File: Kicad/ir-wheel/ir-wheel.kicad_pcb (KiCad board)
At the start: 2 copper layers, 58 x 25 mm, 10 parts, among them IC1 TTE-OPB606, IC2 TTE-OPB606, K1 MOLEX-MICRO-LATCH-03-RIGHT-AN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, K2 MOLEX-MICRO-LATCH-03-RIGHT-AN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

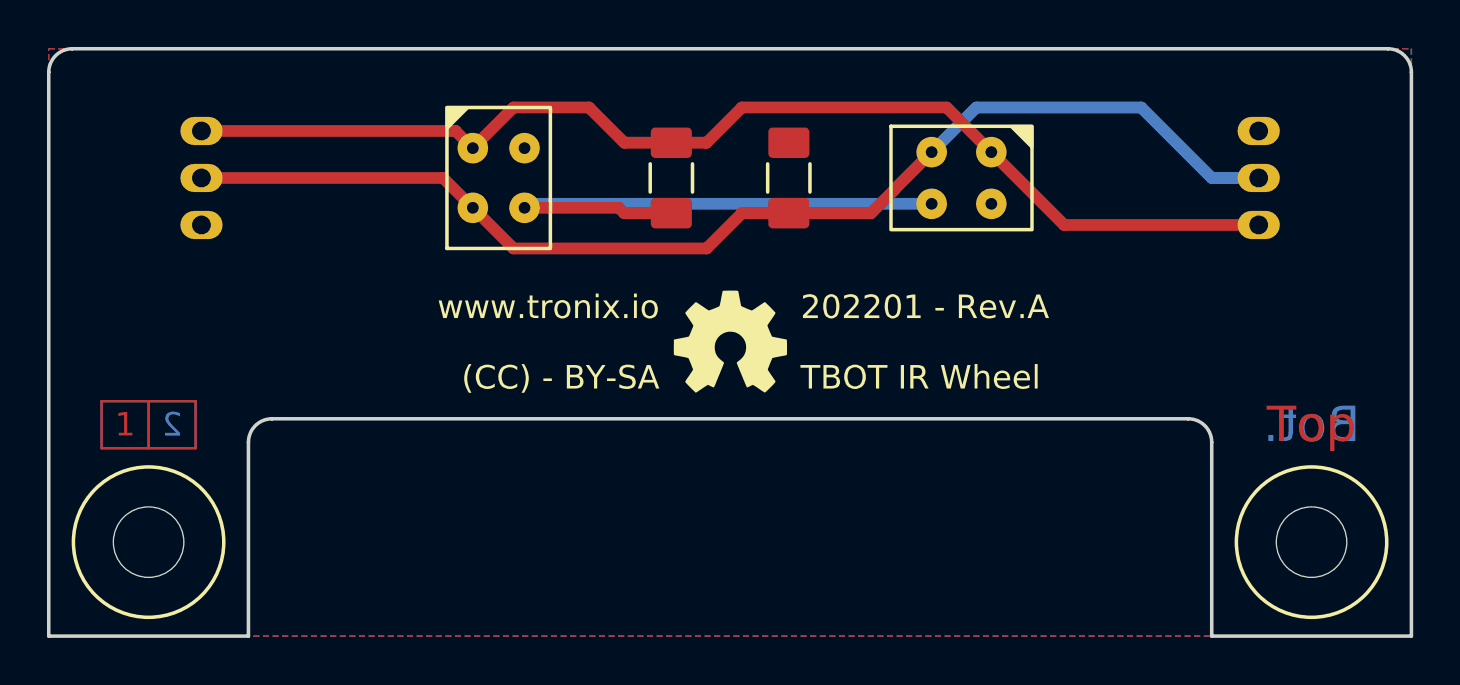
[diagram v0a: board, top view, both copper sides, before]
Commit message: Add IR Wheel
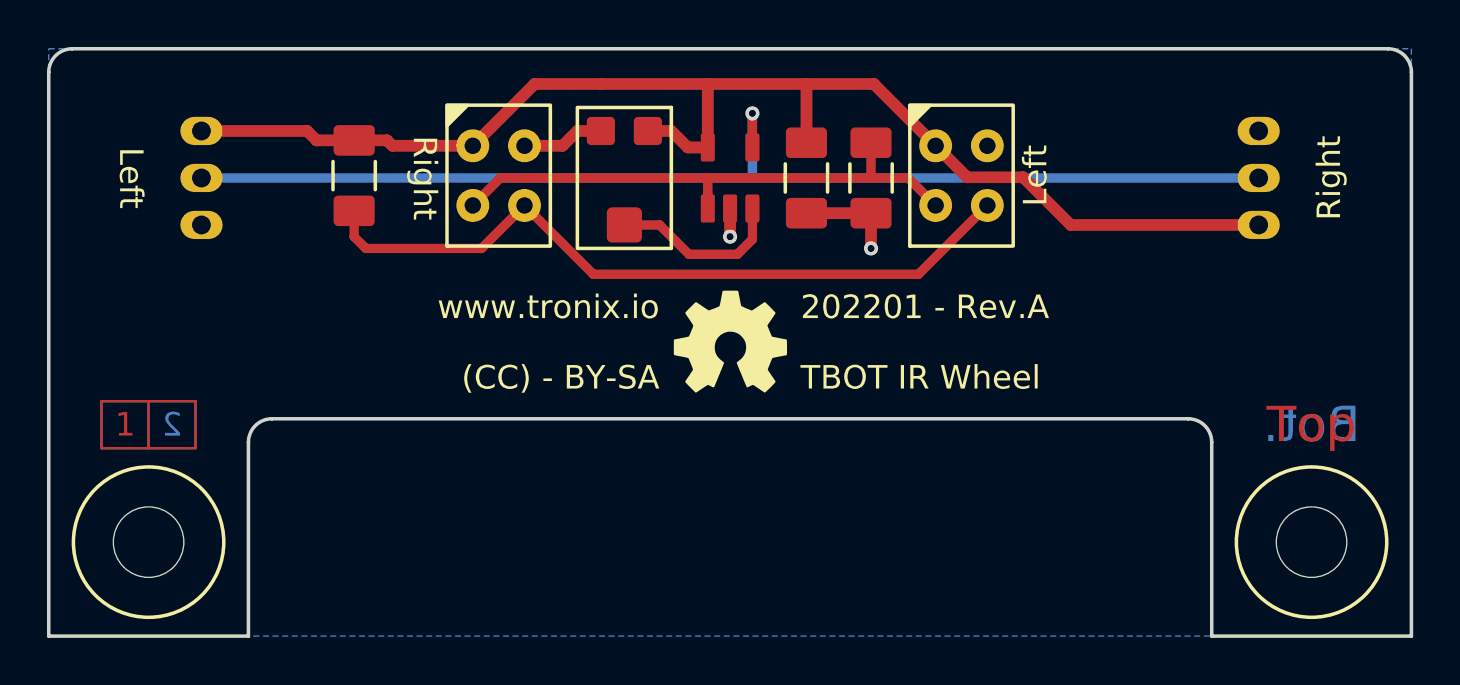
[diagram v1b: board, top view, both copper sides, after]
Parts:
- added C1: 100n, tronixio:CAPACITOR-1206, F.Cu at (132.2, 80.5)
- added P1: BOURNS-TC33X-1K, tronixio:zzzTC33X, F.Cu at (124.5, 80.5)
- added U1: MICROCHIP-MCP6541-SOT-23, tronixio:SOT-23-5, F.Cu at (129.0, 80.5)
- IC1, IC2: footprint tronixio:zzzOPB-606 -> tronixio:zzOPB-606
- moved K1 45.2 mm to (106.5, 78.5), turned to -90 degrees
- moved K2 45.2 mm to (151.5, 82.5), turned to 90 degrees
- moved R1 13.5 mm to (113.0, 80.4)
- moved R2 3.50 mm to (135.0, 80.5), turned to 90 degrees
- moved IC1 0.10 mm to (119.2, 80.4)
- moved IC2 0.10 mm to (138.8, 80.4), turned to 0 degrees
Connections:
- K1 pad 2: Net-(IC1-Pad4) -> Net-(K1-Pad2)
- K2 pad 2: Net-(IC1-Pad4) -> Net-(K1-Pad2)
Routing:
- net Net-(K1-Pad2): track 0.00 -> 49.2 mm, vias 0 -> 1
- net Net-(IC1-Pad4): track 50.0 -> 23.5 mm
- net GND: track 0.00 -> 8.96 mm, vias 0 -> 2
- net Net-(IC1-Pad1): track 23.5 -> 31.4 mm
- net +5V: track 49.3 -> 56.9 mm
- net Net-(U1-Pad3): track 0.00 -> 7.54 mm
- removed copper zone on F.Cu, net GND
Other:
- board text added: "IC2: update y+1 19.5 -> 19.6"
- board text added: "Left"
- board text added: "OPB606: update dirll 0,5 -> .7"
- board text added: "Right"

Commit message: Update IR WHEEL
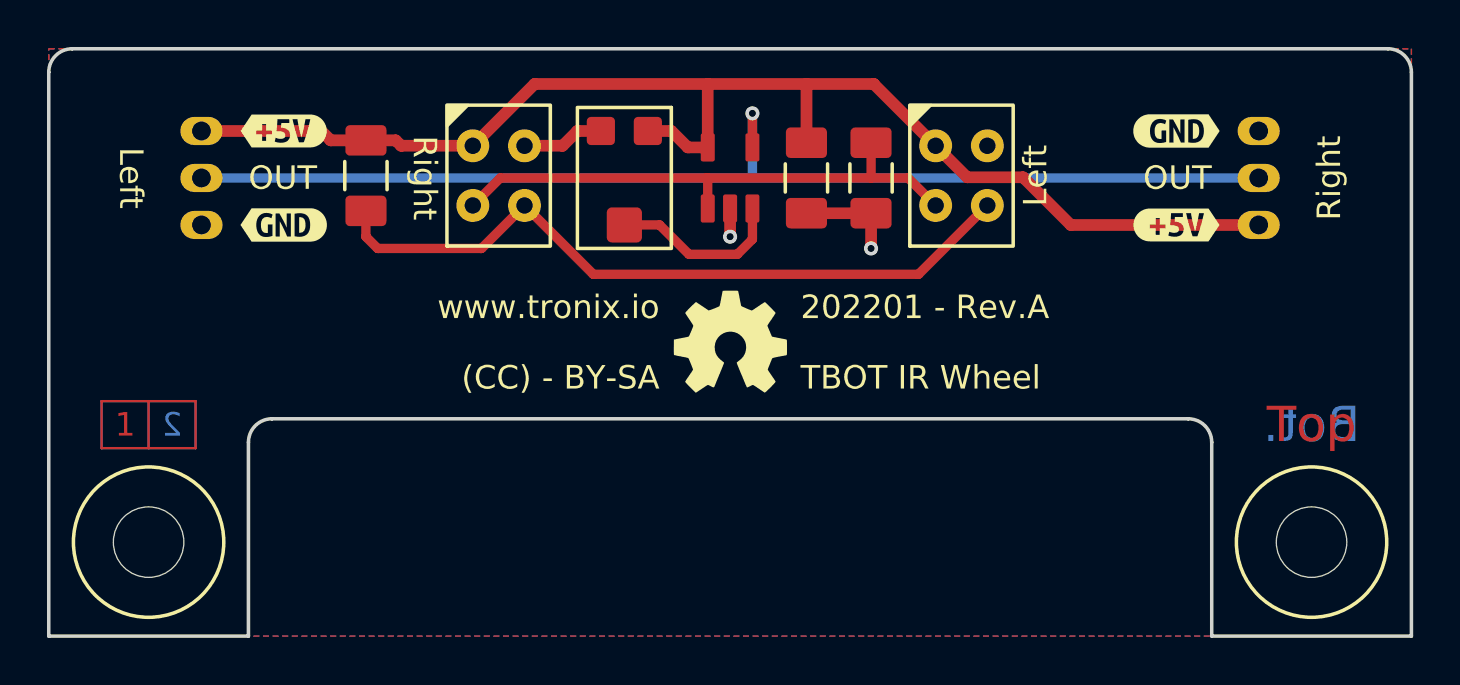
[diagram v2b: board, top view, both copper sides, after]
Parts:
- added kibuzzard-627E9F99: G***, kibuzzard-627E9F99, F.Cu at (110.0, 82.5)
- added kibuzzard-627EA1B6: G***, kibuzzard-627EA1B6, F.Cu at (110.0, 78.5)
- added kibuzzard-627EA1D4: G***, kibuzzard-627EA1D4, F.Cu at (148.0, 78.5)
- added kibuzzard-627EA1EB: G***, kibuzzard-627EA1EB, F.Cu at (148.0, 82.5)
- K1: value MOLEX-MICRO-LATCH-03-RIGHT-ANGLE -> RIGHT
- K2: value MOLEX-MICRO-LATCH-03-RIGHT-ANGLE -> LEFT
- moved R1 0.50 mm to (113.5, 80.4)
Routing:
- added copper zone on F.Cu, net GND
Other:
- board text added: "OUT"

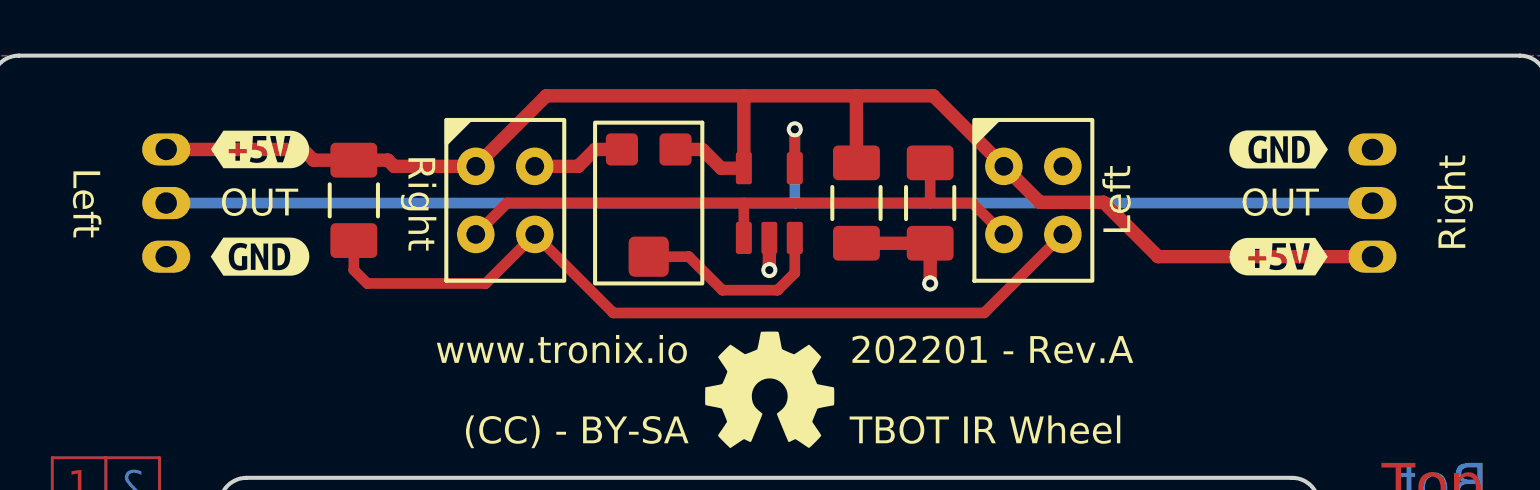
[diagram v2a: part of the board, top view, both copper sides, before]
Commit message: Update IR WHEEL
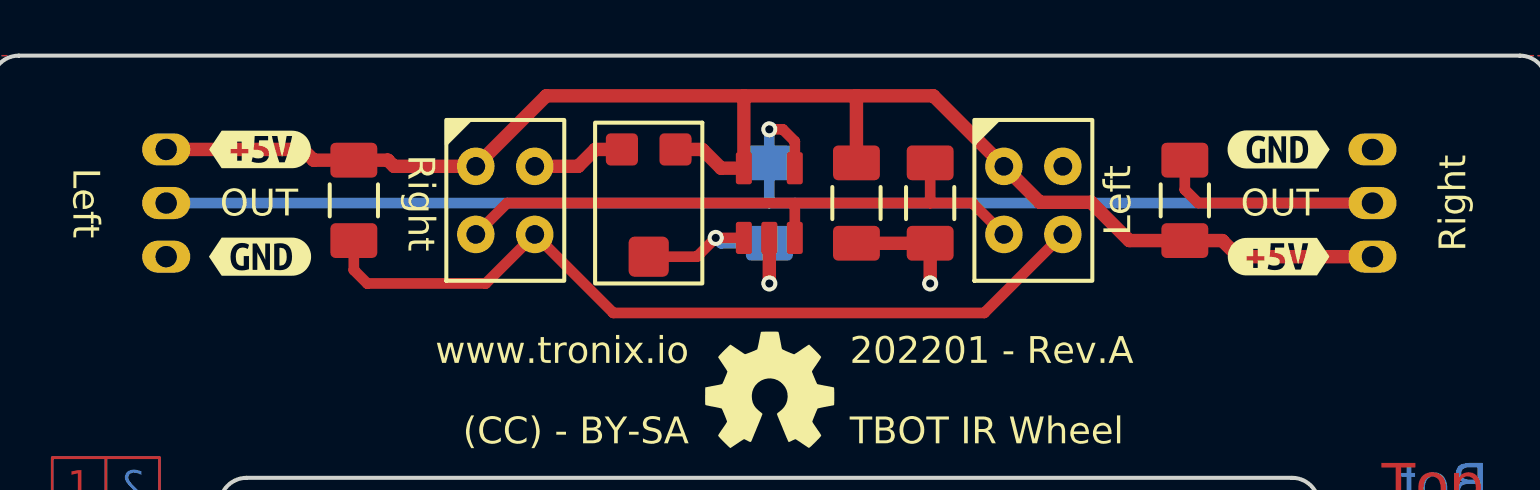
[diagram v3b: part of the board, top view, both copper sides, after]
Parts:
- removed kibuzzard-627E9F99: G***, kibuzzard-627E9F99
- removed kibuzzard-627EA1B6: G***, kibuzzard-627EA1B6
- removed kibuzzard-627EA1D4: G***, kibuzzard-627EA1D4
- removed kibuzzard-627EA1EB: G***, kibuzzard-627EA1EB
- added R3: 10K, tronixio:RESISTOR-1206, F.Cu at (144.5, 80.4)
- added R4: 10K, tronixio:RESISTOR-1206, B.Cu at (129.0, 80.5)
- added kibuzzard-62813E44: G***, kibuzzard-62813E44, F.Cu at (110.0, 82.5)
- added kibuzzard-62813E52: G***, kibuzzard-62813E52, F.Cu at (110.0, 78.5)
- added kibuzzard-62813E5A: G***, kibuzzard-62813E5A, F.Cu at (148.0, 78.5)
- added kibuzzard-62813E63: G***, kibuzzard-62813E63, F.Cu at (148.0, 82.5)
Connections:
- U1 pad 1: Net-(IC1-Pad4) -> Net-(P1-Pad2)
- U1 pad 3: Net-(P1-Pad2) -> Net-(IC1-Pad4)
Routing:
- net Net-(K1-Pad2): track 49.2 -> 58.2 mm
- net Net-(P1-Pad2): track 7.54 -> 5.92 mm, vias 0 -> 1
- net GND: track 8.96 -> 9.46 mm

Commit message: Update
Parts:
- added C2: 1µ, tronixio:CAPACITOR-1206, B.Cu at (132.2, 80.5)
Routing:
- net +5V: track 56.9 -> 58.4 mm, vias 0 -> 1
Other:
- board text removed: "OPB606: update dirll 0,5 -> .7"
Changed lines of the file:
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@@
     (attr board_only exclude_from_pos_files exclude_from_bom)
     (fp_text reference "kibuzzard-62813E52" (at 0 -3.748088) (layer "F.SilkS") hide
-      (effects (font (size 0 0)))
+      (effects (font (size 0 0) (thickness 0.15)))
     )
     (fp_text value "G***" (at 0 3.748088) (layer "F.SilkS") hide
-      (effects (font (size 0 0)))
+      (effects (font (size 0 0) (thickness 0.15)))
     )
     (fp_poly (pts
@@
     (attr board_only exclude_from_pos_files exclude_from_bom)
     (fp_text reference "kibuzzard-62813E5A" (at 0 -3.7592) (layer "F.SilkS") hide
-      (effects (font (size 0 0)))
+      (effects (font (size 0 0) (thickness 0.15)))
     )
     (fp_text value "G***" (at 0 3.7592) (layer "F.SilkS") hide
-      (effects (font (size 0 0)))
+      (effects (font (size 0 0) (thickness 0.15)))
     )
     (fp_poly (pts
@@
     (attr board_only exclude_from_pos_files exclude_from_bom)
     (fp_text reference "kibuzzard-62813E44" (at 0 -3.7592) (layer "F.SilkS") hide
-      (effects (font (size 0 0)))
+      (effects (font (size 0 0) (thickness 0.15)))
     )
     (fp_text value "G***" (at 0 3.7592) (layer "F.SilkS") hide
-      (effects (font (size 0 0)))
+      (effects (font (size 0 0) (thickness 0.15)))
     )
     (fp_poly (pts
@@
     (attr board_only exclude_from_pos_files exclude_from_bom)
     (fp_text reference "kibuzzard-62813E63" (at 0 -3.748088) (layer "F.SilkS") hide
-      (effects (font (size 0 0)))
+      (effects (font (size 0 0) (thickness 0.15)))
     )
     (fp_text value "G***" (at 0 3.748088) (layer "F.SilkS") hide
-      (effects (font (size 0 0)))
+      (effects (font (size 0 0) (thickness 0.15)))
     )
     (fp_poly (pts
@@
     )
   )
+  (footprint "tronixio:CAPACITOR-1206" (layer "B.Cu")
+    (at 132.25 80.5 -90)
+    (property "Sheetfile" "ir-wheel.kicad_sch")
+    (property "Sheetname" "")
+    (zone_connect 2)
+    (attr smd)
+    (fp_text reference "C2" (at 0 2 90) (layer "B.Fab")
+      (effects (font (size 1 1) (thickness 0.15)) (justify mirror))
+    )
+    (fp_text value "1µ" (at 0 -2 90) (layer "B.Fab")
+      (effects (font (size 1 1) (thickness 0.15)) (justify mirror))
+    )
+    (fp_line (start -0.6 0.9) (end 0.6 0.9) (layer "B.SilkS") (width 0.15))
+    (fp_line (start -0.6 -0.9) (end 0.6 -0.9) (layer "B.SilkS") (width 0.15))
+    (fp_rect (start -2.3 -1) (end 2.3 1) (layer "B.CrtYd") (width 0.05) (fill none))
+    (fp_rect (start 1.2 -0.8) (end 1.5 0.8) (layer "B.Fab") (width 0.1) (fill solid))
+    (fp_rect (start -1.2 -0.8) (end 1.2 0.8) (layer "B.Fab") (width 0.1) (fill none))
+    (fp_rect (start -1.5 -0.8) (end -1.2 0.8) (layer "B.Fab") (width 0.1) (fill solid))
+    (pad "1" smd roundrect (at -1.5 0 270) (size 1.3 1.75) (layers "B.Cu" "B.Paste" "B.Mask") (roundrect_rratio 0.15)
+      (net 2 "+5V") (pintype "passive") (zone_connect 2))
+    (pad "2" smd roundrect (at 1.5 0 270) (size 1.3 1.75) (layers "B.Cu" "B.Paste" "B.Mask") (roundrect_rratio 0.15)
+      (net 1 "GND") (pintype "passive") (zone_connect 1))
+    (model "${KICAD6_USER_3DMODEL_DIR}/SMD/CAPACITOR-1206.wrl"
+      (offset (xyz 0 0 0))
+      (scale (xyz 1 1 1))
+      (rotate (xyz 0 0 0))
+    )
+  )
   (footprint "tronixio:M3-MASK" locked (layer "B.Cu")
     (at 153.75 96 180)
@@
     (at 151.5 82.5 90)
     (property "MOUSER" "538-53254-0370")
+    (property "Mouser" "538-53254-0370")
     (property "Sheetfile" "ir-wheel.kicad_sch")
     (property "Sheetname" "")
@@
     (at 106.5 78.5 -90)
     (property "MOUSER" "538-53254-0370")
+    (property "Mouser" "538-53254-0370")
     (property "Sheetfile" "ir-wheel.kicad_sch")
     (property "Sheetname" "")
@@
     (effects (font (size 1.5 1.5) (thickness 0.2)))
   )
-  (gr_text "OPB606: update dirll 0,5 -> .7" (at 118 68.5) (layer "Dwgs.User")
-    (effects (font (size 1.5 1.5) (thickness 0.2)))
-  )
   (dimension (type aligned) (layer "Dwgs.User")
     (pts (xy 100 75.5) (xy 158 75.5))
@@
   (via (at 135 83.5) (size 0.6) (drill 0.3) (layers "F.Cu" "B.Cu") (net 1))
   (segment (start 139.090489 80.470489) (end 137.75 79.13) (width 0.5) (layer "F.Cu") (net 2))
-  (segment (start 132.25 79) (end 132.25 76.5) (width 0.5) (layer "F.Cu") (net 2))
   (segment (start 120.68 76.5) (end 135.12 76.5) (width 0.5) (layer "F.Cu") (net 2))
+  (segment (start 132.25 79) (end 132.25 77.5) (width 0.5) (layer "F.Cu") (net 2))
+  (segment (start 132.25 77.5) (end 132.25 76.5) (width 0.5) (layer "F.Cu") (net 2))
   (segment (start 142.429511 81.9) (end 144.5 81.9) (width 0.5) (layer "F.Cu") (net 2))
   (segment (start 151.5 82.5) (end 146.5 82.5) (width 0.5) (layer "F.Cu") (net 2))
@@
   (segment (start 118.05 79.13) (end 115 79.13) (width 0.5) (layer "F.Cu") (net 2))
   (segment (start 146.5 82.5) (end 145.9 81.9) (width 0.5) (layer "F.Cu") (net 2))
-  (segment (start 120.25 81.67) (end 123.17952 84.59952) (width 0.4) (layer "F.Cu") (net 3))
-  (segment (start 137.02048 84.59952) (end 139.95 81.67) (width 0.4) (layer "F.Cu") (net 3))
-  (segment (start 123.17952 84.59952) (end 137.02048 84.59952) (width 0.4) (layer "F.Cu") (net 3))
-  (segment (start 114 83.5) (end 113.5 83) (width 0.4) (layer "F.Cu") (net 3))
-  (segment (start 113.5 83) (end 113.5 81.9) (width 0.4) (layer "F.Cu") (net 3))
-  (segment (start 118.42 83.5) (end 114 83.5) (width 0.4) (layer "F.Cu") (net 3))
-  (segment (start 120.25 81.67) (end 118.42 83.5) (width 0.4) (layer "F.Cu") (net 3))
+  (via (at 132.25 77.5) (size 0.6) (drill 0.3) (layers "F.Cu" "B.Cu") (net 2))
+  (segment (start 132.25 79) (end 132.25 77.5) (width 0.5) (layer "B.Cu") (net 2))
+  (segment (start 120.25 81.67) (end 123.17952 84.59952) (width 0.5) (layer "F.Cu") (net 3))
+  (segment (start 137.02048 84.59952) (end 139.95 81.67) (width 0.5) (layer "F.Cu") (net 3))
+  (segment (start 123.17952 84.59952) (end 137.02048 84.59952) (width 0.5) (layer "F.Cu") (net 3))
+  (segment (start 114 83.5) (end 113.5 83) (width 0.5) (layer "F.Cu") (net 3))
+  (segment (start 113.5 83) (end 113.5 81.9) (width 0.5) (layer "F.Cu") (net 3))
+  (segment (start 118.42 83.5) (end 114 83.5) (width 0.5) (layer "F.Cu") (net 3))
+  (segment (start 120.25 81.67) (end 118.42 83.5) (width 0.5) (layer "F.Cu") (net 3))
   (segment (start 119.22 80.5) (end 135 80.5) (width 0.4) (layer "F.Cu") (net 4))
   (segment (start 136.58 80.5) (end 135 80.5) (width 0.4) (layer "F.Cu") (net 4))
@@
   (segment (start 119.22 80.5) (end 118.05 81.67) (width 0.4) (layer "F.Cu") (net 4))
   (segment (start 129.95 81.8) (end 129.95 80.5) (width 0.4) (layer "F.Cu") (net 4))
-  (segment (start 144.5 80) (end 144.5 78.9) (width 0.4) (layer "F.Cu") (net 5))
-  (segment (start 129.95 78.2) (end 129.5 77.75) (width 0.4) (layer "F.Cu") (net 5))
-  (segment (start 129.95 79.2) (end 129.95 78.2) (width 0.4) (layer "F.Cu") (net 5))
-  (segment (start 129.5 77.75) (end 129 77.75) (width 0.4) (layer "F.Cu") (net 5))
-  (segment (start 145 80.5) (end 144.5 80) (width 0.4) (layer "F.Cu") (net 5))
-  (segment (start 151.5 80.5) (end 145 80.5) (width 0.4) (layer "F.Cu") (net 5))
+  (segment (start 144.5 80) (end 144.5 78.9) (width 0.5) (layer "F.Cu") (net 5))
+  (segment (start 129.95 78.2) (end 129.5 77.75) (width 0.5) (layer "F.Cu") (net 5))
+  (segment (start 129.95 79.2) (end 129.95 78.2) (width 0.5) (layer "F.Cu") (net 5))
+  (segment (start 129.5 77.75) (end 129 77.75) (width 0.5) (layer "F.Cu") (net 5))
+  (segment (start 145 80.5) (end 144.5 80) (width 0.5) (layer "F.Cu") (net 5))
+  (segment (start 151.5 80.5) (end 145 80.5) (width 0.5) (layer "F.Cu") (net 5))
   (via (at 129 77.75) (size 0.6) (drill 0.3) (layers "F.Cu" "B.Cu") (net 5))
   (segment (start 129 80.5) (end 151.5 80.5) (width 0.4) (layer "B.Cu") (net 5))
-  (segment (start 129 79) (end 129 77.75) (width 0.4) (layer "B.Cu") (net 5))
+  (segment (start 129 79) (end 129 77.75) (width 0.5) (layer "B.Cu") (net 5))
   (segment (start 129 79) (end 129 80.5) (width 0.4) (layer "B.Cu") (net 5))
   (segment (start 106.5 80.5) (end 129 80.5) (width 0.4) (layer "B.Cu") (net 5))
-  (segment (start 126.3 82.5) (end 127 81.8) (width 0.4) (layer "F.Cu") (net 6))
-  (segment (start 124.5 82.5) (end 126.3 82.5) (width 0.4) (layer "F.Cu") (net 6))
-  (segment (start 128.05 81.8) (end 127 81.8) (width 0.4) (layer "F.Cu") (net 6))
+  (segment (start 126.3 82.5) (end 127 81.8) (width 0.5) (layer "F.Cu") (net 6))
+  (segment (start 124.5 82.5) (end 126.3 82.5) (width 0.5) (layer "F.Cu") (net 6))
+  (segment (start 128.05 81.8) (end 127 81.8) (width 0.5) (layer "F.Cu") (net 6))
   (via (at 127 81.8) (size 0.6) (drill 0.3) (layers "F.Cu" "B.Cu") (net 6))
-  (segment (start 127.2 82) (end 127 81.8) (width 0.4) (layer "B.Cu") (net 6))
-  (segment (start 129 82) (end 127.2 82) (width 0.4) (layer "B.Cu") (net 6))
+  (segment (start 127.2 82) (end 127 81.8) (width 0.5) (layer "B.Cu") (net 6))
+  (segment (start 129 82) (end 127.2 82) (width 0.5) (layer "B.Cu") (net 6))
   (zone (net 1) (net_name "GND") (layers F&B.Cu) (hatch edge 0.508)
     (connect_pads (clearance 0.5))
